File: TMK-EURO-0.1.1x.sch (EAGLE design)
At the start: 43 parts, among them IC1 TL082P, U2 IN, U5 IN, U6 IN, U7 THONKICONNOLD, X1 057-010-1

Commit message: Nets netjes
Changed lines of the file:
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@@
 <junction x="208.28" y="116.84"/>
 <wire x1="208.28" y1="116.84" x2="208.28" y2="132.08" width="0.1524" layer="91"/>
-<wire x1="208.28" y1="132.08" x2="246.38" y2="132.08" width="0.1524" layer="91"/>
-<wire x1="246.38" y1="132.08" x2="266.7" y2="132.08" width="0.1524" layer="91"/>
-<wire x1="266.7" y1="132.08" x2="271.78" y2="132.08" width="0.1524" layer="91"/>
 <pinref part="R13" gate="G$1" pin="2"/>
-<wire x1="271.78" y1="132.08" x2="241.3" y2="132.08" width="0.1524" layer="91"/>
+<wire x1="208.28" y1="132.08" x2="241.3" y2="132.08" width="0.1524" layer="91"/>
 </segment>
 </net>
@@
 </segment>
 </net>
-<net name="N$17" class="0">
-<segment>
-<pinref part="R13" gate="G$1" pin="1"/>
-<pinref part="VR12" gate="G$1" pin="E"/>
-<wire x1="251.46" y1="132.08" x2="259.08" y2="132.08" width="0.1524" layer="91"/>
-</segment>
-</net>
 <net name="N$26" class="2">
 <segment>
@@
 </segment>
 </net>
+<net name="N$4" class="0">
+<segment>
+<pinref part="R13" gate="G$1" pin="1"/>
+<pinref part="VR12" gate="G$1" pin="E"/>
+<wire x1="251.46" y1="132.08" x2="259.08" y2="132.08" width="0.1524" layer="91"/>
+</segment>
+</net>
 </nets>
 </sheet>
 </sheets>
-<errors>
-</errors>
 </schematic>
 </drawing>

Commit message: Buffers!
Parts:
- added C3: 100uF, gm-caps-electro-pol:080
- added D2: 1N5817, MusicThingModular:SMALL_DIODEDO35-7
- added U1, U3: TL072_, EURACK-MASTER-LIB:TL072_
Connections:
- new net -12V: C3.-, D2.A, U1P.V-, U3P.V-
- new net N$15: U1A.+IN, VR1.S
- new net N$17: R14.2, U1B.-IN, U1B.OUT
- new net N$27: R13.2, U3A.-IN, U3A.OUT
- new net N$28: U3B.-IN, U3B.OUT, U7.TIP
- new net N$29: U3B.+IN, VR16.S
- net +12V: now also U1P.V+, U3P.V+
- net GND: now also C3.+
- net N$10: now also U1B.+IN; no longer R14.2
- net N$13: now also U3A.+IN; no longer R13.2
- net N$19: now also R4.1, U1A.-IN, U1A.OUT, VR2.E; no longer U7.TIP, VR16.S
- net N$2: now also D2.C, X1-1.S, X1-2.S; no longer R4.1, VR1.S, VR2.E
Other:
- note added: "buffer in"
- note added: "buffer out"
- moved on the sheet: C10, C7, C9, D7, R13, R14, R8, U5, U6, U7, VR12, VR13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

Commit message: Ready for breadboard v2
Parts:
- removed C10, C9: 100nF, rcl:C-EU050-035X075
- removed R13: 47k, adafruit:R-US_0207/7
- removed R14: 100k, adafruit:R-US_0207/7
- removed U5, U6: IN, MusicThingModular:THONKICONNOLD
- removed VR12: 500k, MusicThingModular:9MM_SNAP-IN_POT_
- removed VR13: 250K, MusicThingModular:9MM_SNAP-IN_POT_
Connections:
- removed net N$10: IC1A.OUT, LED1.A, LED2.C, U1B.+IN, VR10.E, VR10.S
- removed net N$16: R14.1, VR13.E
- removed net N$17: R14.2, U1B.-IN, U1B.OUT
- removed net N$25: C10.2, U6.TIP
- removed net N$27: R13.2, U3A.-IN, U3A.OUT
- removed net N$35: C9.2, U5.TIP
- removed net N$4: R13.1, VR12.E
- removed net OUTPUT1: C10.1, VR13.A, VR13.S
- removed net OUTPUT2: C9.1, VR12.A, VR12.S
- new net N$30: IC1A.OUT, LED1.A, LED2.C, VR10.E, VR10.S
- net GND: no longer U5.SLEEVE, U6.SLEEVE
- net N$13: no longer U3A.+IN
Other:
- note removed: "output stage 1"
- note removed: "output stage 2"
- moved on the sheet: C1, C2, C3, C5, C6, C7, D2, D7, R3, R5, U1A, U2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

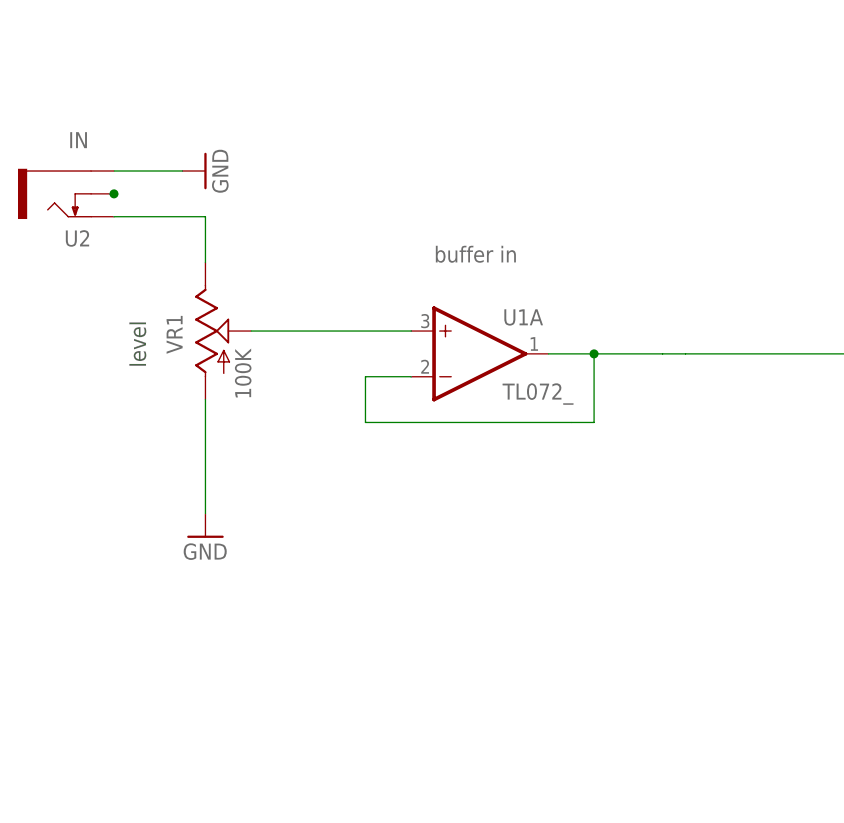
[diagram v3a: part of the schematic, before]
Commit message: Ground switch input jack
Normal to groudn on input switch
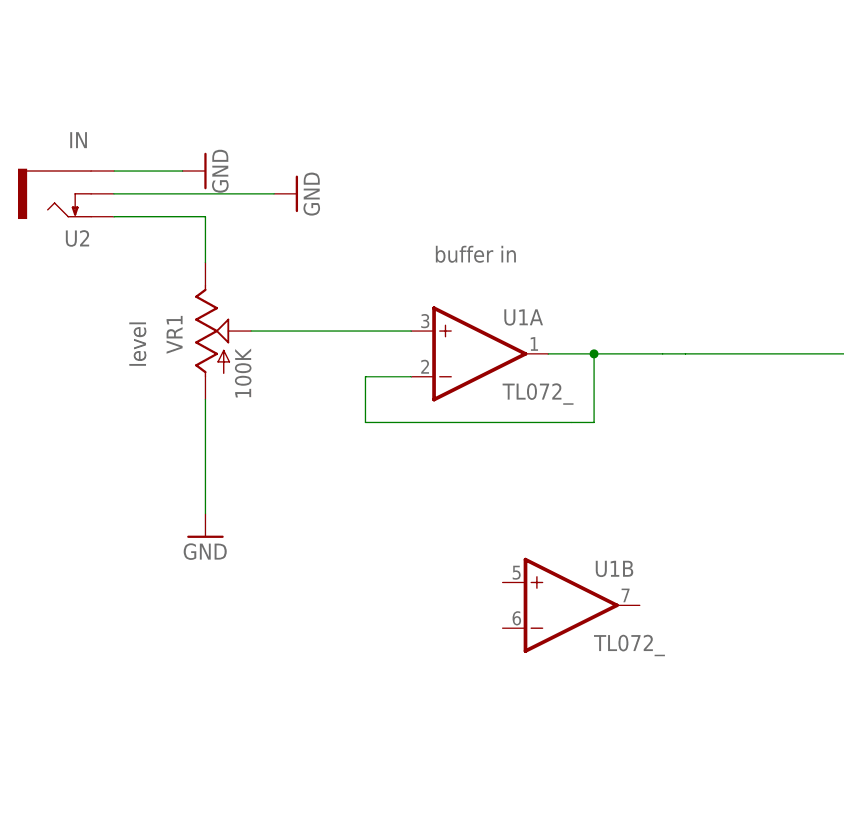
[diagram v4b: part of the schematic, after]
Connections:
- removed net N$1: U2.SWITCH
- net GND: now also U2.SWITCH
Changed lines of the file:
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@@
 <?xml version="1.0" encoding="utf-8"?>
 <!DOCTYPE eagle SYSTEM "eagle.dtd">
-<eagle version="8.2.2">
+<eagle version="7.6.0">
 <drawing>
 <settings>
@@
 </classes>
 <parts>
-<part name="IC1" library="linear" library_urn="urn:adsk.eagle:library:262" deviceset="TL082" device="P"/>
+<part name="IC1" library="linear" deviceset="TL082" device="P"/>
 <part name="R4" library="adafruit" deviceset="R-US_" device="0207/7" value="470"/>
 <part name="R8" library="adafruit" deviceset="R-US_" device="0207/7" value="10K"/>
@@
 <part name="U7" library="MusicThingModular" deviceset="THONKICONN" device="OLD"/>
 <part name="C1" library="adafruit" deviceset="CPOL-US" device="E2-5" value="10uF"/>
-<part name="C4" library="rcl" library_urn="urn:adsk.eagle:library:334" deviceset="C-EU" device="050-035X075" value="100nF"/>
-<part name="C2" library="rcl" library_urn="urn:adsk.eagle:library:334" deviceset="C-EU" device="050-035X075" value="100nF"/>
-<part name="C5" library="rcl" library_urn="urn:adsk.eagle:library:334" deviceset="C-EU" device="050-035X075" value="100nF"/>
+<part name="C4" library="rcl" deviceset="C-EU" device="050-035X075" value="100nF"/>
+<part name="C2" library="rcl" deviceset="C-EU" device="050-035X075" value="100nF"/>
+<part name="C5" library="rcl" deviceset="C-EU" device="050-035X075" value="100nF"/>
 <part name="C6" library="adafruit" deviceset="C-US" device="050-030X075" value="2.2uF"/>
-<part name="GND3" library="supply1" library_urn="urn:adsk.eagle:library:371" deviceset="GND" device=""/>
-<part name="GND4" library="supply1" library_urn="urn:adsk.eagle:library:371" deviceset="GND" device=""/>
-<part name="GND6" library="supply1" library_urn="urn:adsk.eagle:library:371" deviceset="GND" device=""/>
+<part name="GND3" library="supply1" deviceset="GND" device=""/>
+<part name="GND4" library="supply1" deviceset="GND" device=""/>
+<part name="GND6" library="supply1" deviceset="GND" device=""/>
 <part name="VR6" library="gm-supply" deviceset="VR" device=""/>
 <part name="VR5" library="gm-supply" deviceset="VR" device=""/>
 <part name="LED1" library="adafruit" deviceset="LED" device="3MM" value="oranger"/>
 <part name="LED2" library="adafruit" deviceset="LED" device="3MM" value="oranger"/>
-<part name="GND9" library="supply1" library_urn="urn:adsk.eagle:library:371" deviceset="GND" device=""/>
-<part name="GND10" library="supply1" library_urn="urn:adsk.eagle:library:371" deviceset="GND" device=""/>
+<part name="GND9" library="supply1" deviceset="GND" device=""/>
+<part name="GND10" library="supply1" deviceset="GND" device=""/>
 <part name="VR11" library="gm-supply" deviceset="VR" device=""/>
-<part name="GND8" library="supply1" library_urn="urn:adsk.eagle:library:371" deviceset="GND" device=""/>
-<part name="GND7" library="supply1" library_urn="urn:adsk.eagle:library:371" deviceset="GND" device=""/>
-<part name="SUPPLY1" library="supply2" library_urn="urn:adsk.eagle:library:372" deviceset="+12V" device=""/>
+<part name="GND8" library="supply1" deviceset="GND" device=""/>
+<part name="GND7" library="supply1" deviceset="GND" device=""/>
+<part name="SUPPLY1" library="supply2" deviceset="+12V" device=""/>
 <part name="VR4" library="gm-supply" deviceset="VR" device=""/>
-<part name="GND21" library="supply1" library_urn="urn:adsk.eagle:library:371" deviceset="GND" device=""/>
-<part name="GND19" library="supply1" library_urn="urn:adsk.eagle:library:371" deviceset="GND" device=""/>
-<part name="GND20" library="supply1" library_urn="urn:adsk.eagle:library:371" deviceset="GND" device=""/>
-<part name="GND22" library="supply1" library_urn="urn:adsk.eagle:library:371" deviceset="GND" device=""/>
-<part name="GND23" library="supply1" library_urn="urn:adsk.eagle:library:371" deviceset="GND" device=""/>
+<part name="GND21" library="supply1" deviceset="GND" device=""/>
+<part name="GND19" library="supply1" deviceset="GND" device=""/>
+<part name="GND20" library="supply1" deviceset="GND" device=""/>
+<part name="GND22" library="supply1" deviceset="GND" device=""/>
+<part name="GND23" library="supply1" deviceset="GND" device=""/>
 <part name="VR3" library="MusicThingModular" deviceset="9MM_SNAP-IN_POT" device="_" value="1k"/>
-<part name="GND5" library="supply1" library_urn="urn:adsk.eagle:library:371" deviceset="GND" device=""/>
+<part name="GND5" library="supply1" deviceset="GND" device=""/>
 <part name="C11" library="adafruit" deviceset="C-US" device="050-075X075" value="1uF"/>
-<part name="X1" library="con-panduit" library_urn="urn:adsk.eagle:library:169" deviceset="057-010-" device="1"/>
+<part name="X1" library="con-panduit" deviceset="057-010-" device="1"/>
 <part name="D7" library="MusicThingModular" deviceset="SMALL_DIODE" device="DO35-7" value="1N5817"/>
 <part name="C7" library="gm-caps-electro-pol" deviceset="080" device="" value="100uF"/>
-<part name="GND25" library="supply1" library_urn="urn:adsk.eagle:library:371" deviceset="GND" device=""/>
-<part name="GND26" library="supply1" library_urn="urn:adsk.eagle:library:371" deviceset="GND" device=""/>
-<part name="SUPPLY3" library="supply2" library_urn="urn:adsk.eagle:library:372" deviceset="+12V" device=""/>
-<part name="GND27" library="supply1" library_urn="urn:adsk.eagle:library:371" deviceset="GND" device=""/>
-<part name="SUPPLY2" library="supply2" library_urn="urn:adsk.eagle:library:372" deviceset="+12V" device=""/>
+<part name="GND25" library="supply1" deviceset="GND" device=""/>
+<part name="GND26" library="supply1" deviceset="GND" device=""/>
+<part name="SUPPLY3" library="supply2" deviceset="+12V" device=""/>
+<part name="GND27" library="supply1" deviceset="GND" device=""/>
+<part name="SUPPLY2" library="supply2" deviceset="+12V" device=""/>
 <part name="U1" library="EURACK-MASTER-LIB" deviceset="TL072" device="_"/>
 <part name="U3" library="EURACK-MASTER-LIB" deviceset="TL072" device="_"/>
-<part name="SUPPLY4" library="supply2" library_urn="urn:adsk.eagle:library:372" deviceset="+12V" device=""/>
-<part name="SUPPLY5" library="supply2" library_urn="urn:adsk.eagle:library:372" deviceset="+12V" device=""/>
-<part name="SUPPLY6" library="supply2" library_urn="urn:adsk.eagle:library:372" deviceset="-12V" device=""/>
-<part name="SUPPLY7" library="supply2" library_urn="urn:adsk.eagle:library:372" deviceset="-12V" device=""/>
-<part name="SUPPLY8" library="supply2" library_urn="urn:adsk.eagle:library:372" deviceset="-12V" device=""/>
+<part name="SUPPLY4" library="supply2" deviceset="+12V" device=""/>
+<part name="SUPPLY5" library="supply2" deviceset="+12V" device=""/>
+<part name="SUPPLY6" library="supply2" deviceset="-12V" device=""/>
+<part name="SUPPLY7" library="supply2" deviceset="-12V" device=""/>
+<part name="SUPPLY8" library="supply2" deviceset="-12V" device=""/>
 <part name="D2" library="MusicThingModular" deviceset="SMALL_DIODE" device="DO35-7" value="1N5817"/>
 <part name="C3" library="gm-caps-electro-pol" deviceset="080" device="" value="100uF"/>
-<part name="GND1" library="supply1" library_urn="urn:adsk.eagle:library:371" deviceset="GND" device=""/>
+<part name="GND1" library="supply1" deviceset="GND" device=""/>
+<part name="GND2" library="supply1" deviceset="GND" device=""/>
 </parts>
 <sheets>
@@
 <instance part="C3" gate="G$1" x="147.32" y="-20.32" rot="R180"/>
 <instance part="GND1" gate="1" x="147.32" y="-30.48"/>
+<instance part="U1" gate="B" x="-20.32" y="88.9"/>
+<instance part="GND2" gate="1" x="-50.8" y="134.62" rot="R90"/>
 </instances>
 <busses>
@@
 <wire x1="-60.96" y1="132.08" x2="-71.12" y2="132.08" width="0.1524" layer="91"/>
 <pinref part="U2" gate="G$1" pin="TIP"/>
-</segment>
-</net>
-<net name="N$1" class="0">
-<segment>
-<pinref part="U2" gate="G$1" pin="SWITCH"/>
-<junction x="-71.12" y="134.62"/>
 </segment>
 </net>
@@
 <pinref part="C3" gate="G$1" pin="+"/>
 <wire x1="147.32" y1="-27.94" x2="147.32" y2="-22.86" width="0.1524" layer="91"/>
+</segment>
+<segment>
+<pinref part="U2" gate="G$1" pin="SWITCH"/>
+<pinref part="GND2" gate="1" pin="GND"/>
+<wire x1="-71.12" y1="134.62" x2="-53.34" y2="134.62" width="0.1524" layer="91"/>
 </segment>
 </net>
@@
 </schematic>
 </drawing>
-<compatibility>
-<note version="8.2" severity="warning">
-Since Version 8.2, Eagle supports online libraries. The ids
-of those online libraries will not be understood (or retained)
-with this version.
-</note>
-</compatibility>
 </eagle>

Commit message: Buffered Euro Friendly
Ready for tewaking and CV-inputs?
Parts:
- removed C1: 10uF, adafruit:CPOL-USE2-5
- removed R3, R5: 100K, adafruit:R-US_0207/7
- removed VR3: 1k, MusicThingModular:9MM_SNAP-IN_POT_
- C11: value 1uF -> 4.7uF
- IC1: value TL082P -> TL072
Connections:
- removed net N$23: R3.1, VR3.S
- removed net VR: C1.+, IC1B.+IN, R3.2, R5.1, R7.1, R8.2
- net +12V: no longer VR3.E
- net GND: now also IC1B.+IN, R7.1; no longer C1.-, R5.2, VR3.A
- net N$26: no longer VR7.A
- net N$28: now also U1B.-IN, U1B.OUT; no longer U3B.-IN, U3B.OUT
- net N$29: now also U1B.+IN; no longer U3B.+IN
- net N$7: now also VR7.A
- net N$8: now also R8.2
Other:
- note removed: "starvere"
- moved on the sheet: R8, U1B, VR7

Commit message: Add 10k after attenuation
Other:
- note added: "10k!"
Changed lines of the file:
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@@
 <text x="-35.56" y="127" size="1.778" layer="95">buffer in</text>
 <text x="340.36" y="99.06" size="1.778" layer="95">buffer out</text>
+<text x="-50.8" y="121.92" size="1.778" layer="91">10k!</text>
+<text x="292.1" y="91.44" size="1.778" layer="91">10k!</text>
 </plain>
 <instances>

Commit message: Notes
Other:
- note added: "1k!"
- note added: "Bypass!"
- note added: "Is idt zo?"
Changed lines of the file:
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@@
 <?xml version="1.0" encoding="utf-8"?>
 <!DOCTYPE eagle SYSTEM "eagle.dtd">
-<eagle version="8.3.2">
+<eagle version="8.2.2">
 <drawing>
 <settings>
 <setting alwaysvectorfont="yes"/>
-<setting keepoldvectorfont="yes"/>
 <setting verticaltext="up"/>
 </settings>
@@
 <text x="-35.56" y="127" size="1.778" layer="95">buffer in</text>
 <text x="340.36" y="99.06" size="1.778" layer="95">buffer out</text>
-<text x="-50.8" y="121.92" size="1.778" layer="91">10k!</text>
-<text x="292.1" y="91.44" size="1.778" layer="91">10k!</text>
+<text x="-48.26" y="116.84" size="1.778" layer="91">10k!</text>
+<text x="322.58" y="76.2" size="1.778" layer="91">1k!</text>
+<text x="307.34" y="-40.64" size="1.778" layer="91">Is idt zo?</text>
+<text x="320.04" y="-17.78" size="1.778" layer="91">Bypass!</text>
 </plain>
 <instances>

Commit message: FinalCleanUp
Ready for testing, adding CV
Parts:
- removed D4, D5, D6: 1N4148, MusicThingModular:SMALL_DIODEDO35-7
- removed R8: 10K, adafruit:R-US_0207/7
- removed U3: TL072_, EURACK-MASTER-LIB:TL072_
- removed VR10, VR7: 250K, MusicThingModular:9MM_SNAP-IN_POT_
- added C1, C10, C8, C9: 100nF, rcl:C-EU050-035X075
- added R1: 100K, EURACK-MASTER-LIB:RESISTOR7MM
- added R2: 10K, adafruit:R-US_0207/7
- C2: value 100nF -> 56pF
- VR1: value 100K -> 250K
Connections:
- removed net N$21: D4.C, D5.A
- removed net N$22: D5.C, D6.A
- new net N$1: R1.1, VR1.S
- new net N$10: C1.2, C10.1
- new net N$4: R1.2, U1A.+IN
- net +12V: now also C1.1, C8.1; no longer U3P.V+
- net -12V: now also C10.2, C9.2, IC1P.V-; no longer U3P.V-
- net GND: no longer D6.C, IC1P.V-
- net N$15: now also R2.2, U7.TIP; no longer U1A.+IN, VR1.S
- net N$20: no longer D4.A
- net N$28: now also R2.1; no longer U7.TIP
- net N$30: no longer VR10.E, VR10.S
- net N$5: now also C8.2, C9.1; no longer R8.1, VR7.E, VR7.S
- net N$7: no longer VR10.A, VR7.A
- net N$8: no longer R8.2
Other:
- note added: "Chop"
- note added: "Drive-Noise"
- note added: "Lowpass-Bias"
- note added: "tone"
- note removed: "10k!"
- note removed: "1k!"
- note removed: "2"
- note removed: "Bypass!"
- note removed: "Is idt zo?"
- note removed: "LEDcomp"
- note removed: "bias"
- note removed: "feedbackgain"
- note removed: "leakback"
- note removed: "mufflepass"
- note removed: "resonator"
- moved on the sheet: C2, C5, C6, D3, U1A, U1B, VR2, VR8, VR9
